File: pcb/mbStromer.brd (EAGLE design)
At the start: 160.1 x 60.7 mm, 47 parts

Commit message: fixed GND@7912, some optimization..
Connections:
- removed net N$6: C12.1, C16.1, U$1.1
- net GND: now also C12.1, C16.1, U$1.1
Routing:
- net GND: track 25.4 -> 31.4 mm, vias 190 -> 202
- net N$6: track 6.06 -> 0.00 mm
- net -15V: track 55.4 -> 50.8 mm, vias 36 -> 31
- net -12V: track 371.7 -> 371.1 mm
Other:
- board text added: "version 1.0.0"
- board text removed: "version 1.0"
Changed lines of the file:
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@@
 <?xml version="1.0" encoding="utf-8"?>
 <!DOCTYPE eagle SYSTEM "eagle.dtd">
-<eagle version="9.5.2">
+<eagle version="9.6.1">
 <drawing>
 <settings>
@@
 <grid distance="50" unitdist="mil" unit="mil" style="lines" multiple="1" display="no" altdistance="5" altunitdist="mil" altunit="mil"/>
 <layers>
-<layer number="1" name="Top" color="4" fill="1" visible="yes" active="yes"/>
+<layer number="1" name="Top" color="4" fill="1" visible="no" active="yes"/>
 <layer number="2" name="Route2" color="16" fill="1" visible="no" active="no"/>
 <layer number="3" name="Route3" color="17" fill="1" visible="no" active="no"/>
@@
 </layers>
 <board>
-<fusionsync huburn="a.cGVyc29uYWw6dWUyOWM4MzJj" projecturn="a.cGVyc29uYWw6dWUyOWM4MzJjIzIwMTkwNzE5MjA0NDAwNTMx" f3durn="urn:adsk.wipprod:dm.lineage:fb2Qm-O5QTuq7DpXQ8seug" pcbguid="6157593d-bac7-4702-8139-2b79b6df8d29" lastpulledtime="2020-04-04T22:07:24Z" lastsyncedchangeguid="fc057db2-a2db-799a-4d6b-58a8c7eab622"/>
+<fusionsync huburn="a.cGVyc29uYWw6dWUyOWM4MzJj" projecturn="a.cGVyc29uYWw6dWUyOWM4MzJjIzIwMTkwNzE5MjA0NDAwNTMx" f3durn="urn:adsk.wipprod:dm.lineage:fb2Qm-O5QTuq7DpXQ8seug" pcbguid="6157593d-bac7-4702-8139-2b79b6df8d29" lastpulledtime="2020-04-04T22:07:24Z" lastsyncedchangeguid="fc057db2-a2db-799a-4d6b-58a8c7eab622" latestrevisionid="" lastsyncedrevisionid="" lastboardhashguid="" lastpushedtime="" linktopcb3d="%12"/>
 <plain>
 <dimension x1="0" y1="0" x2="160.02" y2="0" x3="80.01" y3="-5.08" textsize="1.778" layer="47"/>
@@
   12V  1.5A
 -12V    .5A</text>
-<text x="77.216" y="31.75" size="0.8128" layer="25" font="vector">version 1.0</text>
+<text x="77.216" y="31.75" size="0.8128" layer="25" font="vector">version 1.0.0</text>
 <wire x1="143.51" y1="26.67" x2="145.415" y2="26.67" width="0.3048" layer="25"/>
 <wire x1="145.415" y1="26.67" x2="145.415" y2="16.383" width="0.3048" layer="25"/>
@@
 <param name="mdViaViaSameLayer" value="6mil"/>
 <param name="mnLayersViaInSmd" value="2"/>
-<param name="mdCopperDimension" value="40mil"/>
+<param name="mdCopperDimension" value="30mil"/>
 <param name="mdDrill" value="12mil"/>
 <param name="mdSmdStop" value="0mil"/>
@@
 <param name="mlViaStopLimit" value="0mil"/>
 <param name="srRoundness" value="0"/>
-<param name="srMinRoundness" value="0mil"/>
+<param name="srMinRoundness" value="2mil"/>
 <param name="srMaxRoundness" value="0mil"/>
 <param name="slThermalIsolate" value="10mil"/>
@@
 <via x="60.96" y="46.99" extent="1-16" drill="0.35"/>
 <via x="58.42" y="46.99" extent="1-16" drill="0.35"/>
+<contactref element="U$1" pad="1"/>
+<contactref element="C12" pad="1"/>
+<contactref element="C16" pad="1"/>
+<wire x1="127" y1="24.13" x2="123.293" y2="24.13" width="1.6256" layer="1"/>
+<wire x1="123.293" y1="24.13" x2="123.19" y2="24.233" width="1.6256" layer="1"/>
+<wire x1="123.19" y1="24.233" x2="123.19" y2="26.44" width="1.6256" layer="1"/>
+<via x="106.934" y="13.335" extent="1-16" drill="0.35"/>
+<via x="108.585" y="13.335" extent="1-16" drill="0.35"/>
+<via x="107.696" y="15.113" extent="1-16" drill="0.35"/>
+<via x="109.22" y="15.113" extent="1-16" drill="0.35"/>
+<via x="152.4" y="19.05" extent="1-16" drill="0.35"/>
+<via x="152.4" y="16.51" extent="1-16" drill="0.35"/>
+<via x="120.65" y="34.29" extent="1-16" drill="0.35"/>
+<via x="119.38" y="34.29" extent="1-16" drill="0.35"/>
+<via x="118.11" y="34.29" extent="1-16" drill="0.35"/>
+<via x="116.84" y="34.29" extent="1-16" drill="0.35"/>
+<via x="115.57" y="34.29" extent="1-16" drill="0.35"/>
+<via x="118.11" y="35.56" extent="1-16" drill="0.35"/>
 </signal>
 <signal name="+15V" class="2">
@@
 <contactref element="U$1" pad="2"/>
 <contactref element="L2" pad="1"/>
-<wire x1="111.76" y1="16.51" x2="104.14" y2="16.51" width="3.2512" layer="1"/>
-<wire x1="115.57" y1="20.32" x2="115.2525" y2="20.0025" width="3.2512" layer="1"/>
-<wire x1="115.2525" y1="20.0025" x2="111.76" y2="16.51" width="3.2512" layer="1"/>
-<wire x1="104.14" y1="16.51" x2="104.14" y2="16.17" width="3.2512" layer="1"/>
-<wire x1="115.57" y1="20.32" x2="115.57" y2="21.25" width="3.2512" layer="1"/>
-<wire x1="115.57" y1="33.655" x2="115.57" y2="38.735" width="3.2512" layer="1"/>
 <wire x1="115.57" y1="38.735" x2="115.57" y2="40.64" width="3.2512" layer="1"/>
 <wire x1="109.22" y1="32.385" x2="115.57" y2="38.735" width="3.2512" layer="1"/>
-<wire x1="109.22" y1="26.035" x2="109.22" y2="32.385" width="3.2512" layer="1"/>
+<wire x1="109.22" y1="21.25" x2="109.22" y2="32.385" width="3.2512" layer="1"/>
 <wire x1="115.57" y1="40.64" x2="115.465" y2="40.64" width="3.2512" layer="1"/>
-<wire x1="109.22" y1="26.035" x2="115.2525" y2="20.0025" width="3.2512" layer="1"/>
 <wire x1="135.89" y1="24.13" x2="138.43" y2="21.59" width="3.2512" layer="1"/>
-<wire x1="117.475" y1="33.655" x2="115.57" y2="33.655" width="3.2512" layer="1"/>
-<via x="117.475" y="33.655" extent="1-16" drill="0.35"/>
+<via x="124.206" y="31.115" extent="1-16" drill="0.35"/>
 <polygon width="0.4064" layer="16">
 <vertex x="144.78" y="27.94"/>
 <vertex x="144.78" y="15.24"/>
-<vertex x="105.918" y="15.24"/>
-<vertex x="105.918" y="33.02"/>
+<vertex x="115.066721875" y="15.362278125"/>
+<vertex x="107.95" y="22.479"/>
+<vertex x="107.95" y="33.02"/>
 <vertex x="128.27" y="33.02"/>
 <vertex x="133.35" y="27.94"/>
 </polygon>
-<via x="111.76" y="16.51" extent="1-16" drill="0.35"/>
-<via x="113.03" y="17.78" extent="1-16" drill="0.35"/>
-<via x="109.22" y="16.51" extent="1-16" drill="0.35"/>
+<via x="109.347" y="24.13" extent="1-16" drill="0.35"/>
 <via x="135.89" y="22.86" extent="1-16" drill="0.35"/>
 <via x="135.89" y="24.13" extent="1-16" drill="0.35"/>
@@
 <via x="127" y="30.48" extent="1-16" drill="0.35"/>
 <via x="125.73" y="30.48" extent="1-16" drill="0.35"/>
-<via x="106.68" y="16.51" extent="1-16" drill="0.35"/>
-<via x="113.03" y="22.352" extent="1-16" drill="0.35"/>
-<via x="111.76" y="23.368" extent="1-16" drill="0.35"/>
-<via x="110.744" y="24.257" extent="1-16" drill="0.35"/>
-<via x="109.855" y="25.273" extent="1-16" drill="0.35"/>
+<via x="109.347" y="22.733" extent="1-16" drill="0.35"/>
+<via x="109.347" y="25.4" extent="1-16" drill="0.35"/>
 <via x="109.347" y="26.67" extent="1-16" drill="0.35"/>
 <via x="109.347" y="27.94" extent="1-16" drill="0.35"/>
@@
 <via x="109.347" y="30.48" extent="1-16" drill="0.35"/>
 <via x="109.347" y="31.75" extent="1-16" drill="0.35"/>
+<wire x1="104.14" y1="16.17" x2="109.22" y2="21.25" width="3.2512" layer="1"/>
+<wire x1="115.57" y1="21.25" x2="109.22" y2="21.25" width="3.2512" layer="1"/>
+<wire x1="115.57" y1="21.25" x2="110.83" y2="21.25" width="3.2512" layer="1"/>
+<wire x1="110.83" y1="21.25" x2="109.347" y2="22.733" width="3.2512" layer="1"/>
 </signal>
 <signal name="-12V" class="1">
@@
 <wire x1="15.24" y1="17.78" x2="13.6525" y2="19.3675" width="1.6256" layer="1"/>
 <wire x1="13.6525" y1="19.3675" x2="11.43" y2="21.59" width="1.6256" layer="1"/>
-<wire x1="15.24" y1="15.875" x2="15.24" y2="17.78" width="1.6256" layer="1"/>
-<wire x1="17.145" y1="13.97" x2="15.24" y2="15.875" width="1.6256" layer="1"/>
-<wire x1="26.67" y1="13.97" x2="17.145" y2="13.97" width="1.6256" layer="1"/>
+<wire x1="15.24" y1="14.605" x2="15.24" y2="17.78" width="1.6256" layer="1"/>
+<wire x1="15.875" y1="13.97" x2="15.24" y2="14.605" width="1.6256" layer="1"/>
+<wire x1="26.67" y1="13.97" x2="15.875" y2="13.97" width="1.6256" layer="1"/>
 <wire x1="26.67" y1="11.43" x2="26.67" y2="13.97" width="1.6256" layer="1"/>
 <wire x1="13.97" y1="50.8" x2="15.24" y2="50.8" width="1.6256" layer="1"/>
@@
 <wire x1="29.21" y1="13.97" x2="55.245" y2="13.97" width="1.6256" layer="16"/>
 <wire x1="26.67" y1="11.43" x2="29.21" y2="13.97" width="1.6256" layer="16"/>
-<wire x1="102.87" y1="13.97" x2="102.87" y2="11.43" width="1.6256" layer="16"/>
-<wire x1="74.295" y1="13.97" x2="102.87" y2="13.97" width="1.6256" layer="16"/>
+<wire x1="100.838" y1="13.97" x2="102.87" y2="11.43" width="1.6256" layer="16"/>
+<wire x1="74.295" y1="13.97" x2="100.838" y2="13.97" width="1.6256" layer="16"/>
 <wire x1="145.415" y1="36.83" x2="147.955" y2="39.37" width="1.6256" layer="16"/>
 <wire x1="145.415" y1="13.335" x2="145.415" y2="36.83" width="1.6256" layer="16"/>
@@
 <wire x1="119.634" y1="13.97" x2="119.38" y2="13.716" width="0.6096" layer="1"/>
 </signal>
-<signal name="N$6">
-<contactref element="U$1" pad="1"/>
-<contactref element="C12" pad="1"/>
-<contactref element="C16" pad="1"/>
-<wire x1="127" y1="24.13" x2="123.293" y2="24.13" width="1.6256" layer="1"/>
-<wire x1="123.293" y1="24.13" x2="123.19" y2="24.233" width="1.6256" layer="1"/>
-<wire x1="123.19" y1="24.233" x2="123.19" y2="26.44" width="1.6256" layer="1"/>
-</signal>
 <signal name="+12V_2" class="1">

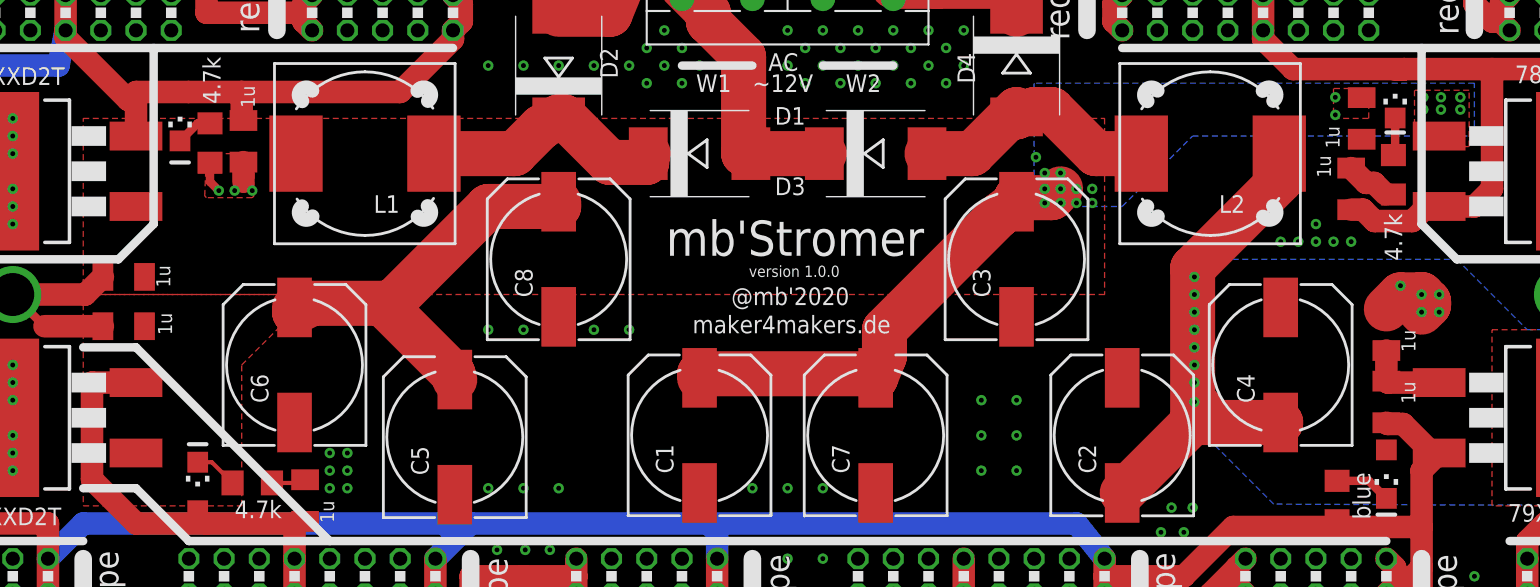
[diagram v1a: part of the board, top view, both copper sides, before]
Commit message: Fixes and Heatsink recommendations.
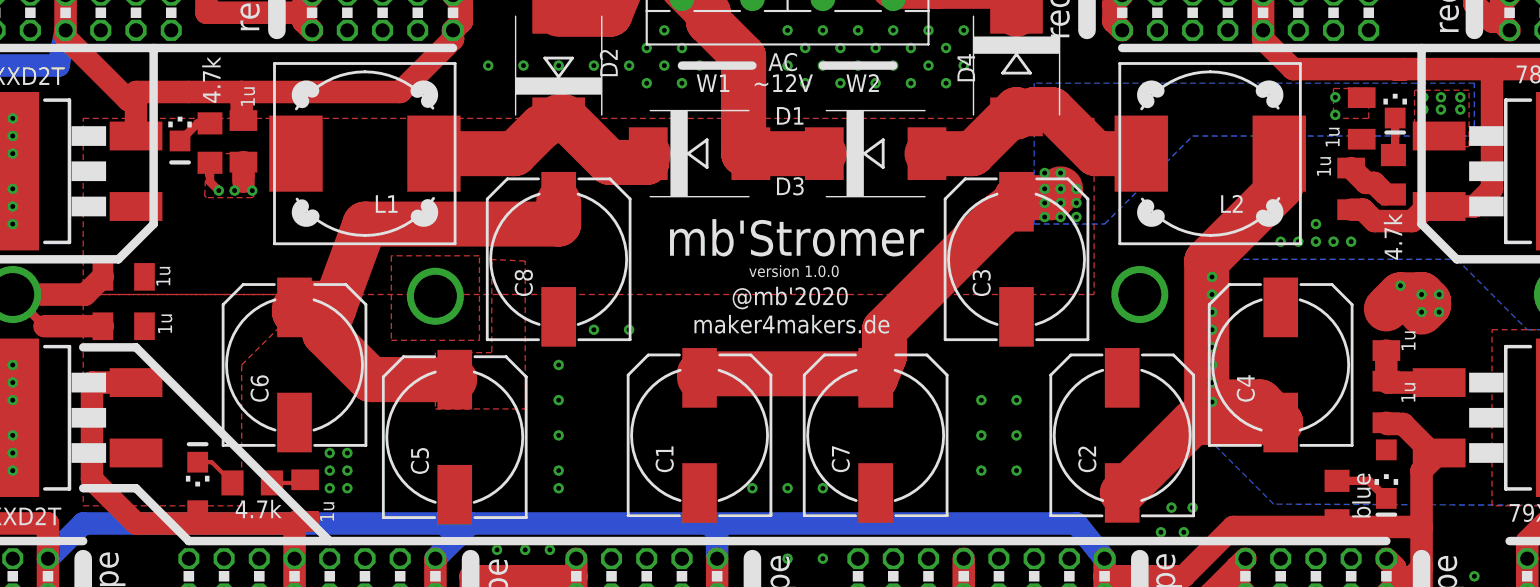
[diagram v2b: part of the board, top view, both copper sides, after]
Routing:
- net +15V: track 64.1 -> 72.1 mm
- net -15V: track 50.8 -> 49.1 mm
- net GND: vias 202 -> 204
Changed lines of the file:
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@@
 <grid distance="50" unitdist="mil" unit="mil" style="lines" multiple="1" display="no" altdistance="5" altunitdist="mil" altunit="mil"/>
 <layers>
-<layer number="1" name="Top" color="4" fill="1" visible="no" active="yes"/>
+<layer number="1" name="Top" color="4" fill="1" visible="yes" active="yes"/>
 <layer number="2" name="Route2" color="16" fill="1" visible="no" active="no"/>
 <layer number="3" name="Route3" color="17" fill="1" visible="no" active="no"/>
@@
 <layer number="45" name="Holes" color="7" fill="1" visible="yes" active="yes"/>
 <layer number="46" name="Milling" color="3" fill="1" visible="no" active="yes"/>
-<layer number="47" name="Measures" color="7" fill="1" visible="no" active="yes"/>
+<layer number="47" name="Measures" color="7" fill="1" visible="yes" active="yes"/>
 <layer number="48" name="Document" color="7" fill="1" visible="no" active="yes"/>
 <layer number="49" name="Reference" color="7" fill="1" visible="no" active="yes"/>
@@
 <wire x1="0" y1="55.88" x2="0" y2="5.08" width="0.254" layer="20"/>
 <wire x1="0" y1="5.08" x2="5.08" y2="0" width="0.254" layer="20" curve="100"/>
+<dimension x1="135.89" y1="30.48" x2="105.41" y2="30.48" x3="120.65" y3="31.75" textsize="1.778" layer="47"/>
+<dimension x1="24.13" y1="30.48" x2="54.61" y2="30.48" x3="39.37" y3="33.02" textsize="1.778" layer="47"/>
+<wire x1="135.89" y1="30.48" x2="102.87" y2="30.48" width="0.254" layer="47"/>
 </plain>
 <attributes>
@@
 <via x="68.58" y="27.94" extent="1-16" drill="0.35"/>
 <via x="66.04" y="27.94" extent="1-16" drill="0.35"/>
-<via x="60.96" y="27.94" extent="1-16" drill="0.35"/>
-<via x="58.42" y="27.94" extent="1-16" drill="0.35"/>
+<via x="63.5" y="22.86" extent="1-16" drill="0.35"/>
+<via x="63.5" y="25.4" extent="1-16" drill="0.35"/>
 <via x="93.98" y="22.86" extent="1-16" drill="0.35"/>
 <via x="93.98" y="20.32" extent="1-16" drill="0.35"/>
@@
 <via x="80.01" y="8.89" extent="1-16" drill="0.35"/>
 <via x="77.47" y="8.89" extent="1-16" drill="0.35"/>
-<via x="58.42" y="16.51" extent="1-16" drill="0.35"/>
-<via x="60.96" y="16.51" extent="1-16" drill="0.35"/>
+<via x="63.5" y="20.32" extent="1-16" drill="0.35"/>
+<via x="63.5" y="17.78" extent="1-16" drill="0.35"/>
 <via x="63.5" y="16.51" extent="1-16" drill="0.35"/>
 <via x="59.055" y="8.255" extent="1-16" drill="0.35"/>
@@
 <via x="115.57" y="34.29" extent="1-16" drill="0.35"/>
 <via x="118.11" y="35.56" extent="1-16" drill="0.35"/>
+<via x="105.41" y="30.48" extent="1-16" drill="3.0988"/>
+<via x="54.61" y="30.353" extent="1-16" drill="3.0988"/>
+<polygon width="0.6096" layer="1" rank="3">
+<vertex x="51.435" y="33.274"/>
+<vertex x="51.435" y="27.178"/>
+<vertex x="57.785" y="27.178"/>
+<vertex x="57.785" y="33.274"/>
+</polygon>
 </signal>
 <signal name="+15V" class="2">
@@
 <wire x1="86.36" y1="24.765" x2="86.36" y2="24.47" width="3.2512" layer="1"/>
 <wire x1="44.45" y1="29.21" x2="44.45" y2="29.55" width="3.2512" layer="1"/>
-<wire x1="50.8" y1="29.845" x2="51.1175" y2="29.5275" width="3.2512" layer="1"/>
-<wire x1="51.1175" y1="29.5275" x2="55.88" y2="24.765" width="3.2512" layer="1"/>
-<wire x1="45.72" y1="29.845" x2="50.8" y2="29.845" width="3.2512" layer="1"/>
-<wire x1="55.88" y1="24.765" x2="56.007" y2="24.343" width="3.2512" layer="1"/>
+<wire x1="46.99" y1="29.845" x2="47.3075" y2="29.5275" width="3.2512" layer="1"/>
+<wire x1="56.007" y1="24.343" x2="49.952" y2="24.343" width="3.2512" layer="1"/>
+<wire x1="49.952" y1="24.343" x2="46.623653125" y2="27.671346875" width="3.2512" layer="1"/>
+<wire x1="45.72" y1="29.845" x2="46.99" y2="29.845" width="3.2512" layer="1"/>
 <wire x1="45.72" y1="29.845" x2="44.45" y2="29.21" width="3.2512" layer="1"/>
-<wire x1="58.42" y1="36.83" x2="63.5" y2="36.83" width="3.2512" layer="1"/>
-<wire x1="51.1175" y1="29.5275" x2="58.42" y2="36.83" width="3.2512" layer="1"/>
-<wire x1="63.5" y1="36.83" x2="63.5" y2="37.17" width="3.2512" layer="1"/>
+<wire x1="49.53" y1="35.56" x2="63.5" y2="35.56" width="3.2512" layer="1"/>
+<wire x1="46.623653125" y1="27.671346875" x2="47.3075" y2="29.5275" width="3.2512" layer="1"/>
+<wire x1="47.3075" y1="29.5275" x2="49.53" y2="35.56" width="3.2512" layer="1"/>
+<wire x1="63.5" y1="35.56" x2="63.5" y2="37.17" width="3.2512" layer="1"/>
 <wire x1="86.995" y1="27.94" x2="95.25" y2="36.195" width="3.2512" layer="1"/>
 <wire x1="86.995" y1="26.035" x2="86.995" y2="27.94" width="3.2512" layer="1"/>
@@
 <via x="125.857" y="44.704" extent="1-16" drill="0.35"/>
 <via x="99.695" y="38.1" extent="1-16" drill="0.35"/>
-<polygon width="0.6096" layer="1" isolate="0.6096" rank="3">
+<polygon width="0.6096" layer="1" isolate="0.6096" rank="4">
 <vertex x="29.21" y="43.18"/>
-<vertex x="102.87" y="43.18"/>
-<vertex x="102.87" y="30.48"/>
+<vertex x="102.108" y="43.18"/>
+<vertex x="102.108" y="30.48"/>
 <vertex x="29.21" y="30.48"/>
 </polygon>
@@
 <polygon width="0.6096" layer="16">
 <vertex x="97.79" y="45.72"/>
-<vertex x="97.79" y="36.83"/>
-<vertex x="104.14" y="36.83"/>
+<vertex x="97.79" y="35.56"/>
+<vertex x="102.87" y="35.56"/>
 <vertex x="109.22" y="41.91"/>
 <vertex x="129.54" y="41.91"/>
@@
 <vertex x="129.159" y="45.212"/>
 </polygon>
-<via x="97.917" y="40.386" extent="1-16" drill="0.35"/>
+<via x="100.838" y="36.068" extent="1-16" drill="0.35"/>
 <via x="99.695" y="37.084" extent="1-16" drill="0.35"/>
 <via x="98.552" y="38.1" extent="1-16" drill="0.35"/>
@@
 <via x="100.838" y="37.084" extent="1-16" drill="0.35"/>
 <via x="100.838" y="38.1" extent="1-16" drill="0.35"/>
-<via x="101.981" y="37.084" extent="1-16" drill="0.35"/>
-<via x="101.981" y="38.1" extent="1-16" drill="0.35"/>
+<via x="98.552" y="36.068" extent="1-16" drill="0.35"/>
+<via x="99.695" y="36.068" extent="1-16" drill="0.35"/>
 <via x="125.857" y="43.815" extent="1-16" drill="0.35"/>
 <via x="127.127" y="43.815" extent="1-16" drill="0.35"/>
 <via x="128.524" y="43.815" extent="1-16" drill="0.35"/>
 <via x="99.695" y="39.243" extent="1-16" drill="0.35"/>
+<polygon width="0.6096" layer="1">
+<vertex x="58.674" y="33.00790625"/>
+<vertex x="58.674" y="26.289"/>
+<vertex x="54.61" y="26.289"/>
+<vertex x="54.61" y="22.225"/>
+<vertex x="61.087" y="22.225"/>
+<vertex x="61.087" y="32.893"/>
+</polygon>
 </signal>
 <signal name="-15V" class="2">
@@
 <contactref element="U$1" pad="2"/>
 <contactref element="L2" pad="1"/>
-<wire x1="115.57" y1="38.735" x2="115.57" y2="40.64" width="3.2512" layer="1"/>
-<wire x1="109.22" y1="32.385" x2="115.57" y2="38.735" width="3.2512" layer="1"/>
-<wire x1="109.22" y1="21.25" x2="109.22" y2="32.385" width="3.2512" layer="1"/>
+<wire x1="115.57" y1="38.227" x2="115.57" y2="40.64" width="3.2512" layer="1"/>
+<wire x1="110.236" y1="32.893" x2="115.57" y2="38.227" width="3.2512" layer="1"/>
+<wire x1="110.236" y1="21.25" x2="110.236" y2="32.893" width="3.2512" layer="1"/>
 <wire x1="115.57" y1="40.64" x2="115.465" y2="40.64" width="3.2512" layer="1"/>
 <wire x1="135.89" y1="24.13" x2="138.43" y2="21.59" width="3.2512" layer="1"/>
@@
 <vertex x="144.78" y="15.24"/>
 <vertex x="115.066721875" y="15.362278125"/>
-<vertex x="107.95" y="22.479"/>
-<vertex x="107.95" y="33.02"/>
+<vertex x="108.712" y="21.717"/>
+<vertex x="108.712" y="33.02"/>
 <vertex x="128.27" y="33.02"/>
 <vertex x="133.35" y="27.94"/>
 </polygon>
-<via x="109.347" y="24.13" extent="1-16" drill="0.35"/>
+<via x="110.617" y="24.13" extent="1-16" drill="0.35"/>
 <via x="135.89" y="22.86" extent="1-16" drill="0.35"/>
 <via x="135.89" y="24.13" extent="1-16" drill="0.35"/>
@@
 <via x="127" y="30.48" extent="1-16" drill="0.35"/>
 <via x="125.73" y="30.48" extent="1-16" drill="0.35"/>
-<via x="109.347" y="22.733" extent="1-16" drill="0.35"/>
-<via x="109.347" y="25.4" extent="1-16" drill="0.35"/>
-<via x="109.347" y="26.67" extent="1-16" drill="0.35"/>
-<via x="109.347" y="27.94" extent="1-16" drill="0.35"/>
-<via x="109.347" y="29.21" extent="1-16" drill="0.35"/>
-<via x="109.347" y="30.48" extent="1-16" drill="0.35"/>
-<via x="109.347" y="31.75" extent="1-16" drill="0.35"/>
+<via x="110.617" y="22.733" extent="1-16" drill="0.35"/>
+<via x="110.617" y="25.4" extent="1-16" drill="0.35"/>
+<via x="110.617" y="26.67" extent="1-16" drill="0.35"/>
+<via x="110.617" y="27.94" extent="1-16" drill="0.35"/>
+<via x="110.617" y="29.21" extent="1-16" drill="0.35"/>
+<via x="110.617" y="30.48" extent="1-16" drill="0.35"/>
+<via x="110.617" y="31.75" extent="1-16" drill="0.35"/>
 <wire x1="104.14" y1="16.17" x2="109.22" y2="21.25" width="3.2512" layer="1"/>
-<wire x1="115.57" y1="21.25" x2="109.22" y2="21.25" width="3.2512" layer="1"/>
-<wire x1="115.57" y1="21.25" x2="110.83" y2="21.25" width="3.2512" layer="1"/>
-<wire x1="110.83" y1="21.25" x2="109.347" y2="22.733" width="3.2512" layer="1"/>
+<wire x1="109.22" y1="21.25" x2="110.236" y2="21.25" width="3.2512" layer="1"/>
+<wire x1="110.236" y1="21.25" x2="115.57" y2="21.25" width="3.2512" layer="1"/>
+<wire x1="115.57" y1="21.25" x2="114.087" y2="22.733" width="3.2512" layer="1"/>
+<wire x1="114.087" y1="22.733" x2="110.617" y2="22.733" width="3.2512" layer="1"/>
 </signal>
 <signal name="-12V" class="1">
